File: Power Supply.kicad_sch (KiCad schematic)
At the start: 8 parts, among them U1 LM317

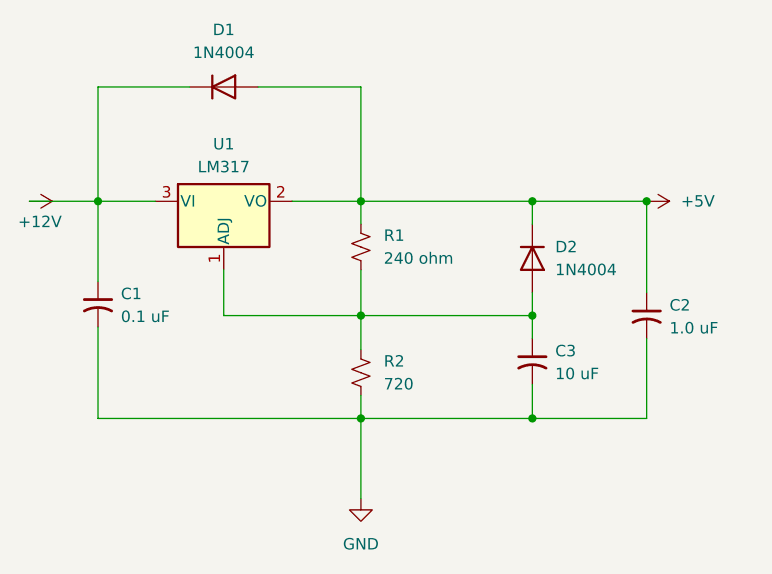
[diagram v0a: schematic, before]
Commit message: - Minor cleanup in the power supply schematic
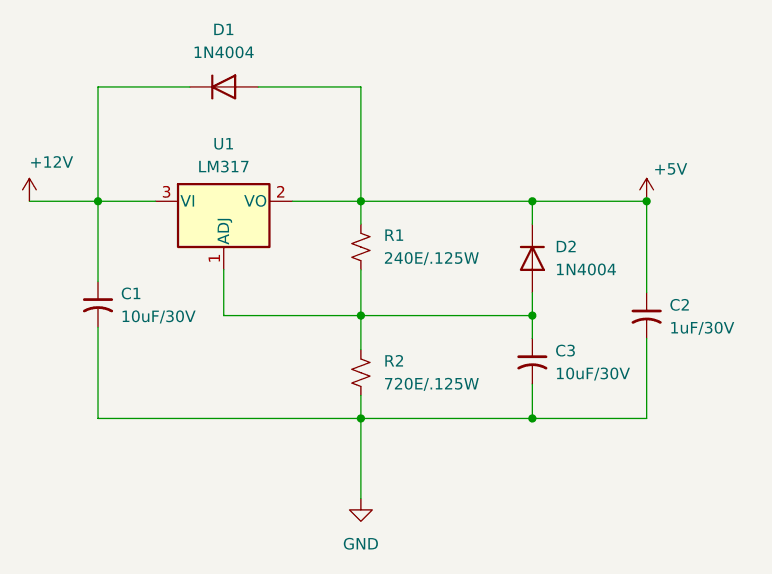
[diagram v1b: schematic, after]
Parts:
- C1: value 0.1 uF -> 10uF/30V
- C2: value 1.0 uF -> 1uF/30V
- C3: value 10 uF -> 10uF/30V
- R1: value 240 ohm -> 240E/.125W
- R2: value 720 -> 720E/.125W
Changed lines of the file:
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@@
 	(symbol
 		(lib_id "power:+12V")
-		(at 100.33 82.55 270)
+		(at 100.33 82.55 0)
 		(unit 1)
 		(exclude_from_sim no)
@@
 		(dnp no)
 		(property "Reference" "#PWR01"
-			(at 96.52 82.55 0)
+			(at 100.33 86.36 0)
 			(effects
 				(font
@@
 		)
 		(property "Value" "+12V"
-			(at 99.06 84.836 90)
+			(at 100.33 78.232 0)
 			(effects
 				(font
@@
 			)
 		)
-		(property "Value" "240 ohm"
+		(property "Value" "240E/.125W"
 			(at 139.7 88.8999 0)
 			(effects
@@
 			)
 		)
-		(property "Value" "720"
+		(property "Value" "720E/.125W"
 			(at 139.7 102.8699 0)
 			(effects
@@
 			)
 		)
-		(property "Value" "0.1 uF"
+		(property "Value" "10uF/30V"
 			(at 110.49 95.3769 0)
 			(effects
@@
 			)
 		)
-		(property "Value" "1.0 uF"
+		(property "Value" "1uF/30V"
 			(at 171.45 96.6469 0)
 			(effects
@@
 	(symbol
 		(lib_id "power:+5V")
-		(at 168.91 82.55 270)
-		(unit 1)
-		(exclude_from_sim no)
-		(in_bom yes)
-		(on_board yes)
-		(dnp no)
-		(fields_autoplaced yes)
+		(at 168.91 82.55 0)
+		(unit 1)
+		(exclude_from_sim no)
+		(in_bom yes)
+		(on_board yes)
+		(dnp no)
 		(property "Reference" "#PWR02"
-			(at 165.1 82.55 0)
+			(at 168.91 86.36 0)
 			(effects
 				(font
@@
 		)
 		(property "Value" "+5V"
-			(at 172.72 82.5499 90)
+			(at 169.672 78.994 0)
 			(effects
 				(font
@@
 			)
 		)
-		(property "Value" "10 uF"
+		(property "Value" "10uF/30V"
 			(at 158.75 101.7269 0)
 			(effects
